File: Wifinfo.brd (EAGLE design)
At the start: 30.5 x 44.5 mm, 40 parts, among them Q1 BS170, U1 CJ1117 3V3

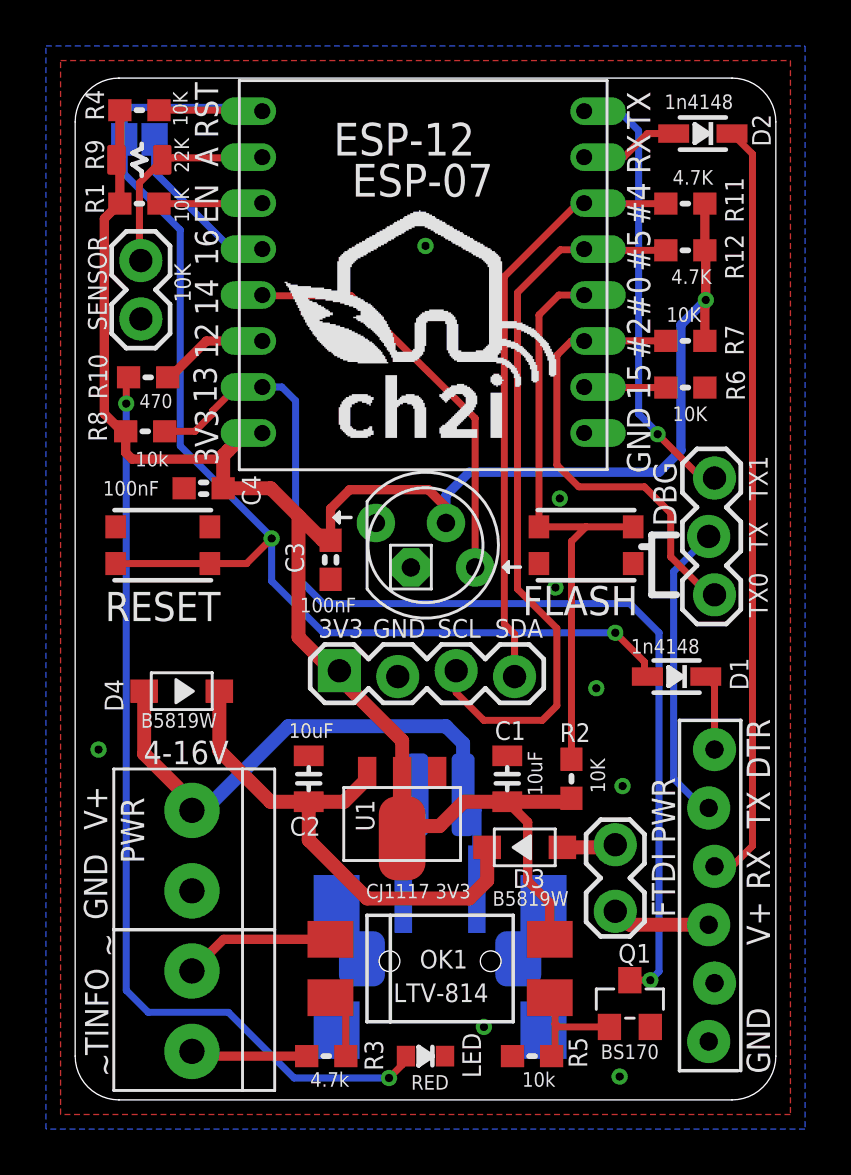
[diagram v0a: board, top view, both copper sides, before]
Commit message: Ajout fonction auto-flash
Ajout fonction auto flash, pour pouvoir flasher le module avec un
adaptateur FTDI like mais sans devoir appuyer sur le bouton flash
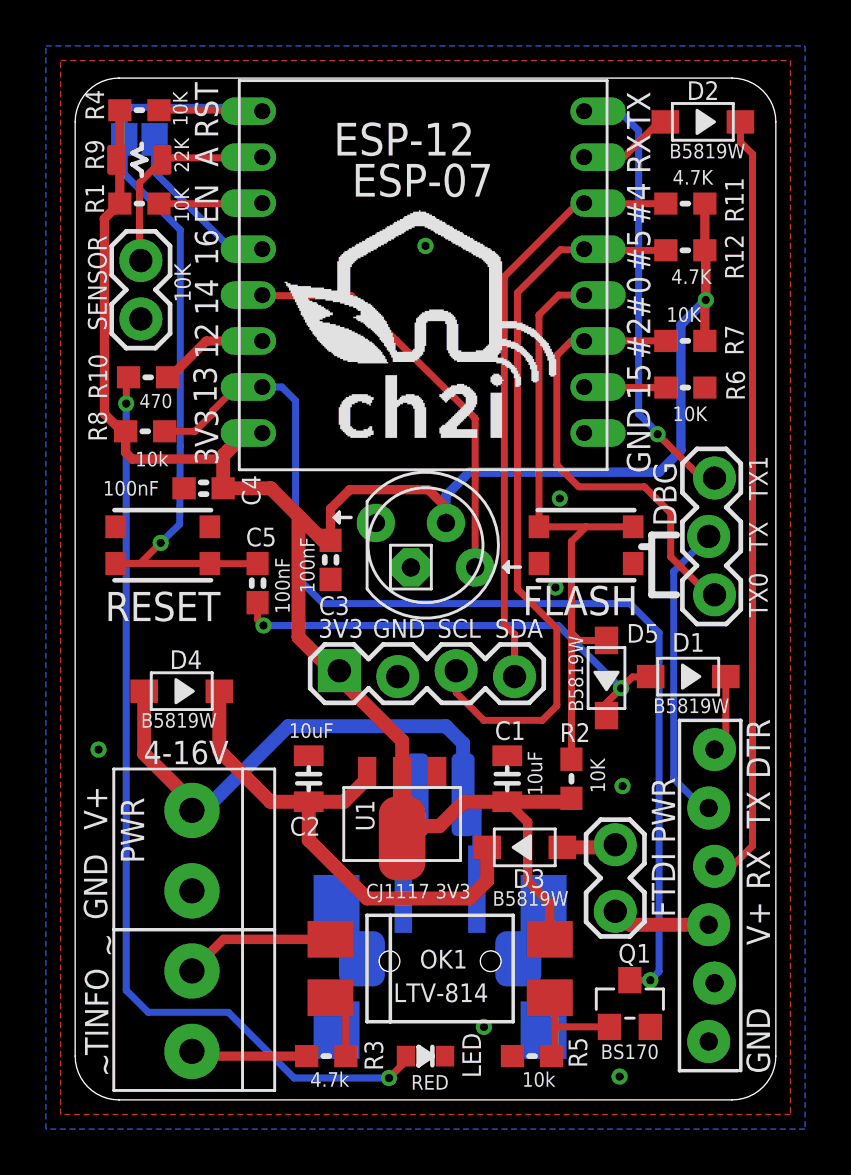
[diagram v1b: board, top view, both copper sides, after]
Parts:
- added C5: 100nF, _c2h:0603-CAP
- added D5: B5819W, Seeed-Discrete:SOD123-2.7X1.6
- D1, D2: value 1n4148 -> B5819W; device microbuilder:SOD-323 -> Seeed-Discrete:SOD123-2.7X1.6
- moved D1 0.51 mm to (26.7, 18.4), turned to 0 degrees
- moved D2 0.51 mm to (27.3, 42.5), turned to 0 degrees
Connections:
- new net N$7: C5.1, D1.1, D5.2
- net DTR_5V: now also D1.2; no longer D1.C
- net GPIO0: now also D5.1
- net RESET: now also C5.2; no longer D1.A
- net RXD1: now also D2.1; no longer D2.A
- net RXD_5V: now also D2.2; no longer D2.C
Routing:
- net RESET: track 59.7 -> 38.3 mm, vias 2 -> 1
- net N$7: track 0.00 -> 20.9 mm, vias 0 -> 2
- net GPIO0: track 26.0 -> 27.7 mm
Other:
- board text added: "To upload firmware with FTDI, close TX-TX0"
- board text added: "Wifinfo V1.0a"
- board text removed: "To upload firmware with FTDI, push flash button when upload and also close TX-TX0"
- board text removed: "Wifinfo V1.0"

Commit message: Minor Adjustments
Minor Adjustments
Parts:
- Q1: value BS170 -> BSS214
- R9: value 22K -> 100K
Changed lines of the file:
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@@
 <?xml version="1.0" encoding="utf-8"?>
 <!DOCTYPE eagle SYSTEM "eagle.dtd">
-<eagle version="6.6.0">
+<eagle version="7.3.0">
 <drawing>
 <settings>
@@
 <setting verticaltext="up"/>
 </settings>
-<grid distance="25" unitdist="mil" unit="mil" style="lines" multiple="1" display="yes" altdistance="2.5" altunitdist="mil" altunit="mil"/>
+<grid distance="50" unitdist="mil" unit="mil" style="lines" multiple="1" display="yes" altdistance="5" altunitdist="mil" altunit="mil"/>
 <layers>
 <layer number="1" name="Top" color="4" fill="1" visible="yes" active="yes"/>
@@
 <pass name="Default">
 <param name="RoutingGrid" value="50mil"/>
+<param name="AutoGrid" value="1"/>
+<param name="Efforts" value="0"/>
+<param name="TopRouterVariant" value="1"/>
 <param name="tpViaShape" value="round"/>
 <param name="PrefDir.1" value="|"/>
@@
 <attribute name="VALUE" x="10.414" y="22.0345" size="0.635" layer="21" font="vector" ratio="15" rot="R90"/>
 </element>
-<element name="R9" library="_c2h" package="0805-RES" value="22K" x="2.794" y="40.894" smashed="yes" rot="R180">
+<element name="R9" library="_c2h" package="0805-RES" value="100K" x="2.794" y="40.894" smashed="yes" rot="R180">
 <attribute name="NAME" x="0.4445" y="41.783" size="0.8128" layer="25" font="vector" ratio="15" rot="R270"/>
 <attribute name="VALUE" x="4.318" y="41.8465" size="0.635" layer="21" font="vector" ratio="15" rot="R270"/>
 </element>
-<element name="Q1" library="Seeed-Discrete" package="SOT23" value="BS170" x="24.13" y="4.191" smashed="yes">
+<element name="Q1" library="Seeed-Discrete" package="SOT23" value="BSS214" x="24.13" y="4.191" smashed="yes">
 <attribute name="NAME" x="23.622" y="5.969" size="0.8128" layer="25" font="vector" ratio="15"/>
-<attribute name="VALUE" x="22.86" y="1.778" size="0.635" layer="21" font="vector" ratio="15"/>
+<attribute name="VALUE" x="22.606" y="1.778" size="0.635" layer="21" font="vector" ratio="15"/>
 </element>
 <element name="R8" library="_c2h" package="0603-RES" value="10k" x="3.048" y="29.083" smashed="yes" rot="R180">
